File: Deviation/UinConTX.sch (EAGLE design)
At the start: 34 parts, among them J1 MICRO_USB_B_MALE_HIROSE_ZX80-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, Q4 8MHz, U1 ATMEGA328L, U2 ###V, U3 HC_05

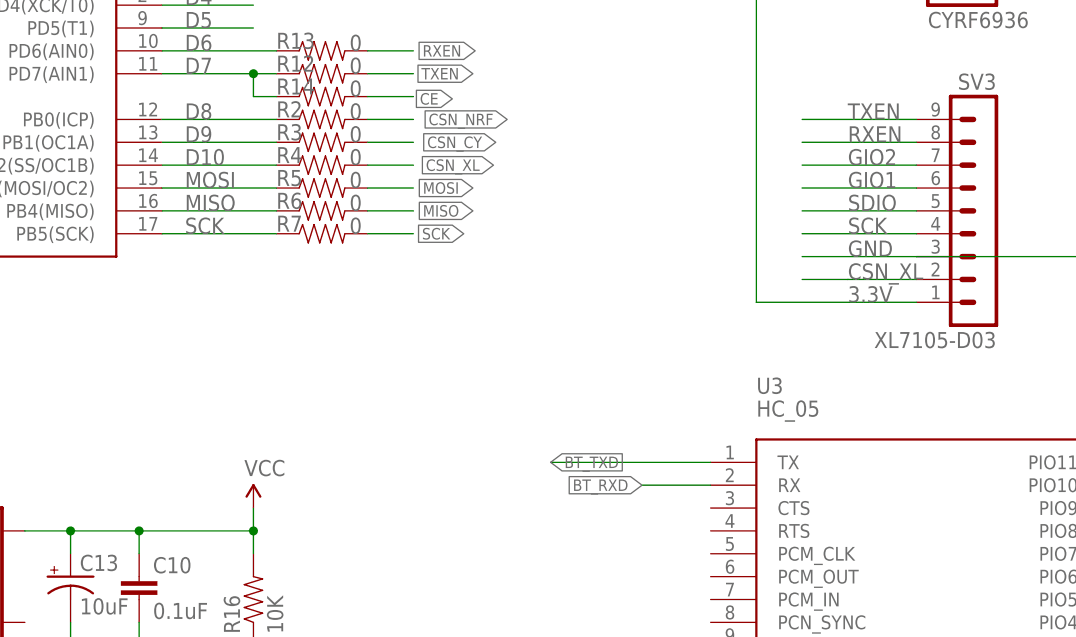
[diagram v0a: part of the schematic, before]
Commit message: Devo protocol added
Schematic is modified for 4-wire SPI for A7105
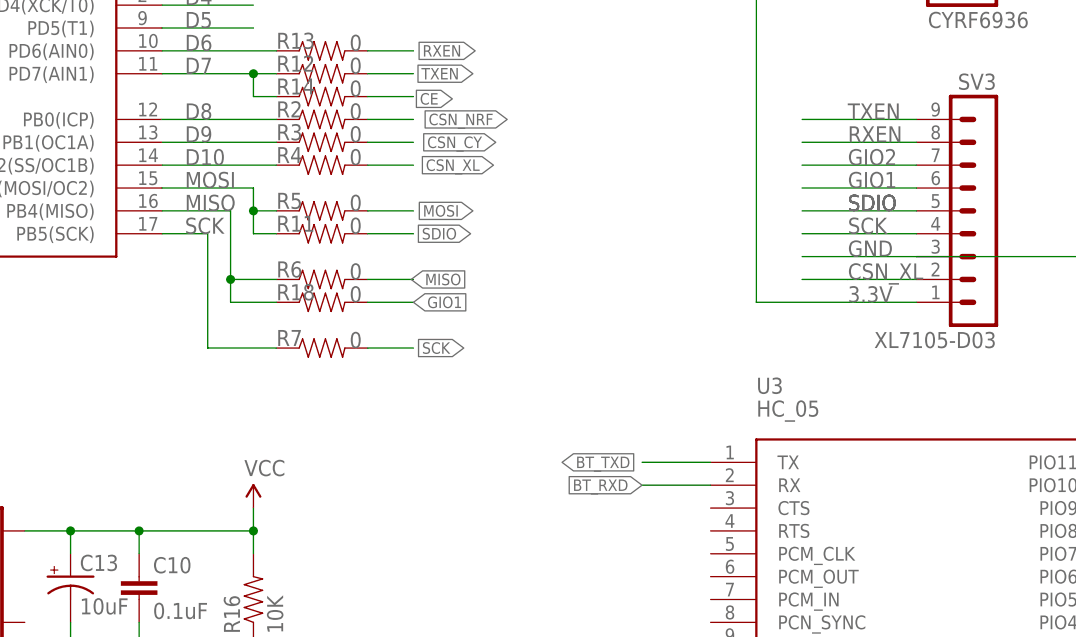
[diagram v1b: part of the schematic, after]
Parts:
- added R11, R18: 0, SparkFun:RESISTOR0402
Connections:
- net GIO1: now also R18.2
- net MISO: now also R18.1
- net MOSI: now also R11.1
- net SDIO: now also R11.2
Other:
- moved on the sheet: R5, R6, R7
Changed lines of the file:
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@@
 <part name="J1" library="connector" deviceset="MICRO_USB_B_MALE_HIROSE_ZX80-B-5S" device=""/>
 <part name="GND1" library="SparkFun" deviceset="GND" device=""/>
+<part name="R11" library="SparkFun" deviceset="RESISTOR" device="0402" value="0"/>
+<part name="R18" library="SparkFun" deviceset="RESISTOR" device="0402" value="0"/>
 </parts>
 <sheets>
@@
 <attribute name="VALUE" x="130.048" y="91.44" size="1.778" layer="96"/>
 </instance>
-<instance part="R5" gate="G$1" x="127" y="88.9" smashed="yes">
-<attribute name="NAME" x="121.92" y="89.1286" size="1.778" layer="95"/>
-<attribute name="VALUE" x="130.048" y="88.9" size="1.778" layer="96"/>
-</instance>
-<instance part="R6" gate="G$1" x="127" y="86.36" smashed="yes">
+<instance part="R5" gate="G$1" x="127" y="86.36" smashed="yes">
 <attribute name="NAME" x="121.92" y="86.5886" size="1.778" layer="95"/>
 <attribute name="VALUE" x="130.048" y="86.36" size="1.778" layer="96"/>
 </instance>
-<instance part="R7" gate="G$1" x="127" y="83.82" smashed="yes">
-<attribute name="NAME" x="121.92" y="84.0486" size="1.778" layer="95"/>
-<attribute name="VALUE" x="130.048" y="83.82" size="1.778" layer="96"/>
+<instance part="R6" gate="G$1" x="127" y="78.74" smashed="yes">
+<attribute name="NAME" x="121.92" y="78.9686" size="1.778" layer="95"/>
+<attribute name="VALUE" x="130.048" y="78.74" size="1.778" layer="96"/>
+</instance>
+<instance part="R7" gate="G$1" x="127" y="71.12" smashed="yes">
+<attribute name="NAME" x="121.92" y="71.3486" size="1.778" layer="95"/>
+<attribute name="VALUE" x="130.048" y="71.12" size="1.778" layer="96"/>
 </instance>
 <instance part="R8" gate="G$1" x="127" y="114.3" smashed="yes">
@@
 <instance part="J1" gate="G$1" x="30.48" y="45.72" rot="MR0"/>
 <instance part="GND1" gate="1" x="45.72" y="33.02"/>
+<instance part="R11" gate="G$1" x="127" y="83.82" smashed="yes">
+<attribute name="NAME" x="121.92" y="84.0486" size="1.778" layer="95"/>
+<attribute name="VALUE" x="130.048" y="83.82" size="1.778" layer="96"/>
+</instance>
+<instance part="R18" gate="G$1" x="127" y="76.2" smashed="yes">
+<attribute name="NAME" x="121.92" y="76.4286" size="1.778" layer="95"/>
+<attribute name="VALUE" x="130.048" y="76.2" size="1.778" layer="96"/>
+</instance>
 </instances>
 <busses>
@@
 <label x="111.76" y="83.82" size="1.778" layer="95"/>
 <pinref part="U1" gate="G$1" pin="PB5(SCK)"/>
-<wire x1="109.22" y1="83.82" x2="121.92" y2="83.82" width="0.1524" layer="91"/>
+<wire x1="109.22" y1="83.82" x2="114.3" y2="83.82" width="0.1524" layer="91"/>
+<wire x1="114.3" y1="83.82" x2="114.3" y2="71.12" width="0.1524" layer="91"/>
+<wire x1="114.3" y1="71.12" x2="121.92" y2="71.12" width="0.1524" layer="91"/>
 <pinref part="R7" gate="G$1" pin="1"/>
 </segment>
@@
 <segment>
 <pinref part="R7" gate="G$1" pin="2"/>
-<wire x1="132.08" y1="83.82" x2="137.16" y2="83.82" width="0.1524" layer="91"/>
-<label x="142.748" y="83.82" size="1.27" layer="95" rot="R180" xref="yes"/>
+<wire x1="132.08" y1="71.12" x2="137.16" y2="71.12" width="0.1524" layer="91"/>
+<label x="142.748" y="71.12" size="1.27" layer="95" rot="R180" xref="yes"/>
 </segment>
 </net>
@@
 <segment>
 <pinref part="U1" gate="G$1" pin="PB4(MISO)"/>
-<wire x1="109.22" y1="86.36" x2="121.92" y2="86.36" width="0.1524" layer="91"/>
+<wire x1="109.22" y1="86.36" x2="116.84" y2="86.36" width="0.1524" layer="91"/>
+<wire x1="116.84" y1="86.36" x2="116.84" y2="78.74" width="0.1524" layer="91"/>
+<wire x1="116.84" y1="78.74" x2="121.92" y2="78.74" width="0.1524" layer="91"/>
 <label x="111.76" y="86.36" size="1.778" layer="95"/>
 <pinref part="R6" gate="G$1" pin="1"/>
+<wire x1="116.84" y1="78.74" x2="116.84" y2="76.2" width="0.1524" layer="91"/>
+<pinref part="R18" gate="G$1" pin="1"/>
+<wire x1="116.84" y1="76.2" x2="121.92" y2="76.2" width="0.1524" layer="91"/>
+<junction x="116.84" y="78.74"/>
 </segment>
 <segment>
 <pinref part="R6" gate="G$1" pin="2"/>
-<wire x1="132.08" y1="86.36" x2="137.16" y2="86.36" width="0.1524" layer="91"/>
-<label x="143.764" y="86.36" size="1.27" layer="95" rot="R180" xref="yes"/>
+<wire x1="132.08" y1="78.74" x2="137.16" y2="78.74" width="0.1524" layer="91"/>
+<label x="136.906" y="78.74" size="1.27" layer="95" xref="yes"/>
 </segment>
 </net>
@@
 <label x="111.76" y="88.9" size="1.778" layer="95"/>
 <pinref part="U1" gate="G$1" pin="PB3(MOSI/OC2)"/>
-<wire x1="109.22" y1="88.9" x2="121.92" y2="88.9" width="0.1524" layer="91"/>
+<wire x1="109.22" y1="88.9" x2="119.38" y2="88.9" width="0.1524" layer="91"/>
+<wire x1="119.38" y1="88.9" x2="119.38" y2="86.36" width="0.1524" layer="91"/>
 <pinref part="R5" gate="G$1" pin="1"/>
+<pinref part="R11" gate="G$1" pin="1"/>
+<wire x1="119.38" y1="86.36" x2="121.92" y2="86.36" width="0.1524" layer="91"/>
+<wire x1="121.92" y1="83.82" x2="119.38" y2="83.82" width="0.1524" layer="91"/>
+<wire x1="119.38" y1="83.82" x2="119.38" y2="86.36" width="0.1524" layer="91"/>
+<junction x="119.38" y="86.36"/>
 </segment>
 <segment>
@@
 <segment>
 <pinref part="R5" gate="G$1" pin="2"/>
-<wire x1="132.08" y1="88.9" x2="137.16" y2="88.9" width="0.1524" layer="91"/>
-<label x="143.764" y="88.9" size="1.27" layer="95" rot="R180" xref="yes"/>
+<wire x1="132.08" y1="86.36" x2="137.16" y2="86.36" width="0.1524" layer="91"/>
+<label x="143.764" y="86.36" size="1.27" layer="95" rot="R180" xref="yes"/>
 </segment>
 </net>
@@
 <wire x1="193.04" y1="86.36" x2="180.34" y2="86.36" width="0.1524" layer="91"/>
 <label x="185.42" y="86.36" size="1.778" layer="95"/>
+<label x="185.42" y="86.36" size="1.778" layer="95"/>
+<label x="185.42" y="86.36" size="1.778" layer="95"/>
+</segment>
+<segment>
+<pinref part="R11" gate="G$1" pin="2"/>
+<wire x1="132.08" y1="83.82" x2="137.16" y2="83.82" width="0.1524" layer="91"/>
+<label x="143.51" y="83.82" size="1.27" layer="95" rot="R180" xref="yes"/>
 </segment>
 </net>
@@
 <wire x1="193.04" y1="88.9" x2="180.34" y2="88.9" width="0.1524" layer="91"/>
 <label x="185.42" y="88.9" size="1.778" layer="95"/>
+</segment>
+<segment>
+<pinref part="R18" gate="G$1" pin="2"/>
+<wire x1="132.08" y1="76.2" x2="137.16" y2="76.2" width="0.1524" layer="91"/>
+<label x="137.16" y="76.2" size="1.27" layer="95" xref="yes"/>
 </segment>
 </net>
@@
 <segment>
 <pinref part="U3" gate="G$1" pin="TX"/>
-<wire x1="170.18" y1="58.42" x2="152.4" y2="58.42" width="0.1524" layer="91"/>
-<label x="152.4" y="58.42" size="1.27" layer="95" xref="yes"/>
-</segment>
-</net>
+<wire x1="170.18" y1="58.42" x2="162.56" y2="58.42" width="0.1524" layer="91"/>
+<label x="153.67" y="58.42" size="1.27" layer="95" xref="yes"/>
+</segment>
+</net>

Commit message: Schematic updated and auto baud rate bug fix
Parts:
- added CA_1, CA_2, CA_4, CR_4: 2.2uF, rc-master-smd:C_0402
- added CA_10: 22pF, rc-master-smd:C_0402
- added CA_11: NC, rc-master-smd:C_0402
- added CA_12, CC_10, CC_11, CS_2, CS_3: 100pF, rc-master-smd:C_0402
- added CA_13, CN_2, CR_5: 10nF, rc-master-smd:C_0402
- added CA_14, CA_15, CS_5: 9pF, rc-master-smd:C_0402
- added CA_16, CA_17, CA_18, CC_12, CC_13, CN_13: 1.0pF, rc-master-smd:C_0402
- added CA_3, CA_6: 10pF, rc-master-smd:C_0402
- added CA_5, CC_1, CC_2, CC_4, CC_5, CS_1: 0.1uF, rc-master-smd:C_0402
- added CA_7: 120pF, rc-master-smd:C_0402
- added CA_8: 1.5nF, rc-master-smd:C_0402
- added CA_9: 680pF, rc-master-smd:C_0402
- added CC_14: 1.8pF, rc-master-smd:C_0402
- added CC_15, CN_12, CY_4: 1.5pF, rc-master-smd:C_0402
- added CC_3, CC_6, CC_9, CR_6: 220pF, rc-master-smd:C_0402
- added CC_7, CC_8, CN_8, CN_9, CY_2: 15pF, rc-master-smd:C_0402
- added CJ_3, CJ_4, CY_3: 2pF, rc-master-smd:C_0402
- added CN_1: 33nF, rc-master-smd:C_0402
- added CN_10: 2.2nF, rc-master-smd:C_0402
- added CN_11: 4.7pF, rc-master-smd:C_0402
- added CN_7: 1nF, rc-master-smd:C_0402
- added CY_1, CY_5: 0.47uF, rc-master-smd:C_0402
- added CY_10, CY_11, CY_12, CY_13, CY_6, CY_7, CY_8, CY_9: 47nF, rc-master-smd:C_0402
- added J3: U.FL, UniversalTx:U.FL
- added LA_2: 4.7nH, rc-master-smd:L_0402
- added LA_3, LC_1, LC_2, LC_3: 1.2nH, rc-master-smd:L_0402
- added LA_4: 3.1nH, rc-master-smd:L_0402
- added LJ_2: 1.5nH, rc-master-smd:L_0402
- added LN_4: 2.7nH, rc-master-smd:L_0402
- added LN_5: 8.2nH, rc-master-smd:L_0402
- added LN_6: 3.9nH, rc-master-smd:L_0402
- added LY_1: 22nH, rc-master-smd:L_0402
- added LY_2: 1.8nH, rc-master-smd:L_0402
- added RA_1: NC, rc-master-smd:R_0402
- added RA_2: 200, rc-master-smd:R_0402
- added RC_1: 56.2k, rc-master-smd:R_0402
- added RN_2: 1M, rc-master-smd:R_0402
- added RN_3: 22k, rc-master-smd:R_0402
- added TP1, TP2, TP4, TP5, TP6, TP7, TP8, TP9: TPTP09R, testpad:TPTP09R
- added TP3: TPB1,27, testpad:TPB1,27
- added UA_1: A7105, UniversalTx:A7105
- added UC_2: CC2500, UniversalTx:CC2500
- added UN_2: NRF24L01, UniversalTx:NRF24L01
- added UR_2: RFX2401C, UniversalTx:RFX2401C
- added US_1: PE42641, UniversalTx:PE42641
- added UY_2: CYRF6936, UniversalTx:CYRF6936
- added YA_1, YN_2: 16MHz, UniversalTx:CRYSTAL.3.2X2.5MM
- added YC_2: 26MHz, UniversalTx:CRYSTAL.3.2X2.5MM
- added YY_2: 12MHz, UniversalTx:CRYSTAL.5X3.2MM
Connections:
- new net +3V3: CA_2.1, CC_2.1, CC_3.1, CC_4.1, CC_5.1, CC_6.1, CC_9.1, CN_2.1, CN_7.1, CR_4.1, CR_5.1, CR_6.1, CS_1.1, CY_1.2, CY_10.1, CY_11.2, CY_12.2, CY_13.1, CY_6.1, CY_7.2, CY_8.1, CY_9.1, UA_1.REGI, UC_2.AVDD_11, UC_2.AVDD_14, UC_2.AVDD_15, UC_2.AVDD_9, UC_2.DGUARD, UC_2.DVDD, UN_2.VDD_15, UN_2.VDD_18, UN_2.VDD_7, UR_2.VDD_14, UR_2.VDD_16, US_1.VDD, UY_2.VBAT0, UY_2.VBAT1, UY_2.VBAT2, UY_2.VCC_16, UY_2.VCC_3, UY_2.VCC_7, UY_2.VIO, UY_2.VREG
- new net A7105_CSN: TP5.TP, UA_1.SCS
- new net CC_CSN: TP3.TP, UC_2.CSN
- new net CYRF_CSN: TP4.TP, UY_2.NCS
- new net MUXSEL1: CS_2.2, TP1.TP, US_1.V2
- new net MUXSEL2: CS_3.1, TP2.TP, US_1.V1
- new net N$18: CN_8.1, RN_2.1, UN_2.XC1, YN_2.2
- new net N$19: CN_9.1, RN_2.2, UN_2.XC2, YN_2.1
- new net N$20: LN_5.1, LN_6.2, UN_2.ANT2
- new net N$21: CN_12.1, LN_6.1
- new net N$22: CN_12.2, CN_13.1, US_1.RF2
- new net N$23: CN_1.1, UN_2.DVDD
- new net N$25: RN_3.1, UN_2.IREF
- new net N$26: CA_9.1, RA_2.2, UA_1.VT
- new net N$27: CA_13.1, RA_2.1
- new net N$28: CA_14.1, UA_1.XO, YA_1.2
- new net N$29: CA_15.1, UA_1.XI, YA_1.1
- new net N$30: CA_4.1, UA_1.DVDD
- new net N$34: CA_7.1, UA_1.RSSI
- new net N$36: CA_8.1, UA_1.BPBG
- new net N$42: CA_10.1, UA_1.RFI
- new net N$48: CA_6.1, LA_3.1, UA_1.RFO
- new net N$49: CA_3.1, RA_1.1, UA_1.VDA2
- new net N$51: CC_1.1, UC_2.DCOUPL
- new net N$52: CC_7.1, UC_2.XOSC_Q2, YC_2.2
- new net N$53: CC_8.1, UC_2.XOSC_Q1, YC_2.1
- new net N$54: RC_1.1, UC_2.RBIAS
- new net N$55: CC_11.2, CC_12.1, LC_2.2
- new net N$56: CC_10.2, CC_13.1, LC_1.2
- new net N$57: CY_1.1, UY_2.RST
- new net N$58: UY_2.XTAL, YY_2.1
- new net N$59: LY_1.2, UY_2.RFBIAS
- new net N$60: CY_2.1, LY_1.1, LY_2.1, UY_2.RF_P
- new net N$61: CY_3.1, LY_2.2, UY_2.RF_N
- new net N$62: CJ_3.1, LJ_2.2, UR_2.ANT
- new net N$63: CA_17.1, CA_18.1, LA_4.1, US_1.RF1
- new net N$64: CA_10.2, CA_16.1, CA_6.2, LA_2.1, LA_4.2
- new net N$65: CC_10.1, UC_2.RF_N
- new net N$66: CC_11.1, UC_2.RF_P
- new net N$67: CC_13.2, CC_14.1, LC_2.1, LC_3.2
- new net N$68: CC_15.1, LC_3.1, US_1.RF4
- new net N$69: CY_2.2, CY_4.1, US_1.RF3
- new net N$70: CJ_4.1, J3.SIGNAL, LJ_2.1
- new net N$71: LN_4.1, LN_5.2, UN_2.ANT1
- new net N$72: CY_5.2, UY_2.VDD
- new net N$73: CS_5.1, US_1.ANT
- new net N$74: CS_5.2, UR_2.TXRX
- new net NRF_CE: UN_2.CE
- new net NRF_CSN: TP7.TP, UN_2.CSN
- new net NRF_PAEN: CN_10.1, CN_11.1, LN_4.2, TP6.TP, UN_2.VDD_PA
- new net RX_EN: TP9.TP, UR_2.RXEN
- new net TX_EN: TP8.TP, UR_2.TXEN
- new net VPLL_7105: CA_1.1, CA_11.1, CA_12.1, CA_5.1, LA_3.2, RA_1.2, UA_1.VDA1, UA_1.VDA3
- new net VSS: CA_1.2, CA_11.2, CA_12.2, CA_13.2, CA_14.2, CA_15.2, CA_16.2, CA_17.2, CA_18.2, CA_2.2, CA_3.2, CA_4.2, CA_5.2, CA_7.2, CA_8.2, CA_9.2, CC_1.2, CC_12.2, CC_14.2, CC_15.2, CC_2.2, CC_3.2, CC_4.2, CC_5.2, CC_6.2, CC_7.2, CC_8.2, CC_9.2, CJ_3.2, CJ_4.2, CN_1.2, CN_10.2, CN_11.2, CN_13.2, CN_2.2, CN_7.2, CN_8.2, CN_9.2, CR_4.2, CR_5.2, CR_6.2, CS_1.2, CS_2.1, CS_3.2, CY_10.2, CY_11.1, CY_12.1, CY_13.2, CY_3.2, CY_4.2, CY_5.1, CY_6.2, CY_7.1, CY_8.2, CY_9.2, J3.GND@0, J3.GND@1, LA_2.2, LC_1.1, RC_1.2, RN_3.2, UA_1.GND_15, UA_1.GND_7, UC_2.VSS_16, UC_2.VSS_19, UN_2.VSS_14, UN_2.VSS_17, UN_2.VSS_20, UN_2.VSS_8, UR_2.VSS_1, UR_2.VSS_11, UR_2.VSS_12, UR_2.VSS_15, UR_2.VSS_2, UR_2.VSS_3, UR_2.VSS_7, UR_2.VSS_8, UR_2.VSS_9, US_1.VSS_1, US_1.VSS_10, US_1.VSS_12, US_1.VSS_14, US_1.VSS_5, US_1.VSS_7, US_1.VSS_9, UY_2.L/D, UY_2.NC_14, UY_2.NC_15, UY_2.NC_17, UY_2.NC_18, UY_2.NC_2, UY_2.NC_20, UY_2.NC_21, UY_2.NC_22, UY_2.NC_23, UY_2.NC_31, UY_2.NC_32, UY_2.NC_36, UY_2.NC_39, UY_2.NC_4, UY_2.NC_5, UY_2.NC_9, UY_2.RESV, UY_2.VSS_12, YA_1.VSS, YC_2.VSS, YN_2.VSS, YY_2.2, YY_2.VSS
- net MISO: now also UA_1.GIO1, UC_2.SO, UN_2.MISO, UY_2.MISO
- net MOSI: now also UA_1.SDIO, UC_2.SI, UN_2.MOSI, UY_2.MOSI
- net SCK: now also UA_1.SCK, UC_2.SCLK, UN_2.SCK, UY_2.SCK
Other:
- note added: "Potential PA/LNA solutions: RDAT212 CC2591 RFX2401C SST12LF03 MCP01 RFX2402C"
- note added: "Y2: 12MHz, 30PPM 60Ohm, 10pF"
- note added: "YA_1: 20PPM, 80ohm, 8pF"
- note added: "YN_1: 60PPM, 100ohm, 8pF RN_1: 1M on BK2423, unneeded on nrf24l01+"
- moved on the sheet: C10, C13, C19, C2, C3, C4, C5, D1, J1, LED1, Q4, R1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
